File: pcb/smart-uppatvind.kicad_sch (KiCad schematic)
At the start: 70 parts, among them J1 PWR, J2 QWIIC, J3 UART_PROG, J4 FAN, Q1 IRLML9301, Q2 MMBT3904, Q3 MMBT3904, Q4 MMBT3904, Q5 Q_NMOS_GSD, SW1 EN, SW2 MAIN, SW3 BOOT, SW4 FILTER, U1 LDL1117S33R, U2 L7980A, U3 ESP32-C3-WROOM-02, U4 M24C02-WMN

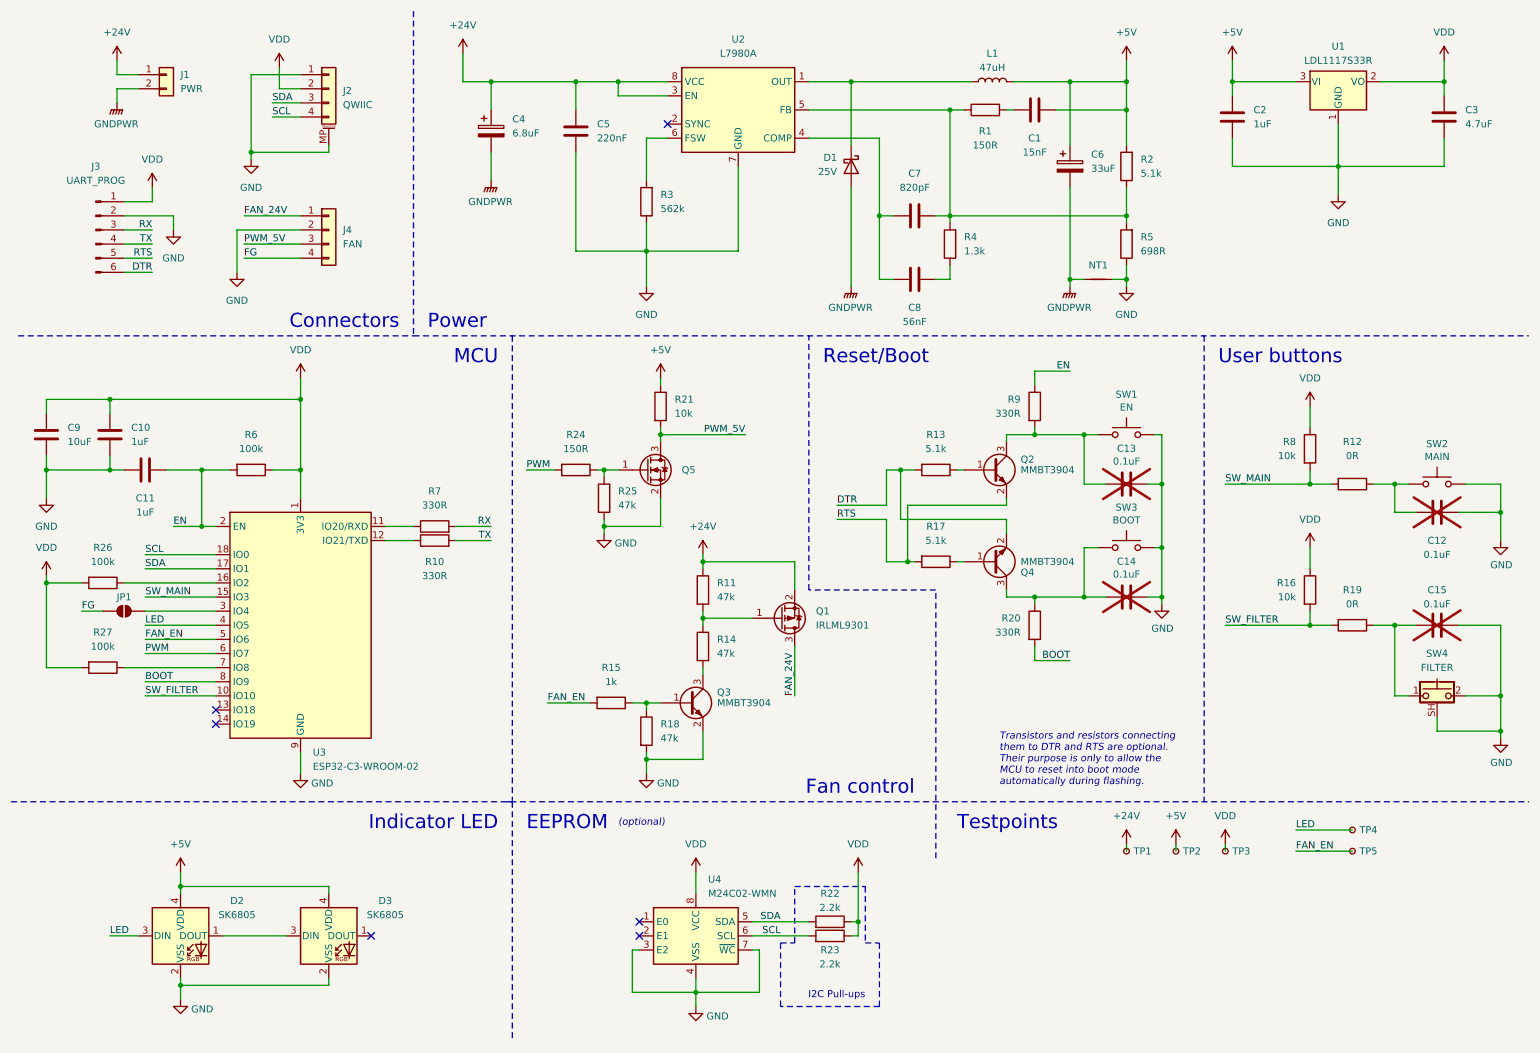
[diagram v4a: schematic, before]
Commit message: Reannotated components geographically, adjusted designator positions
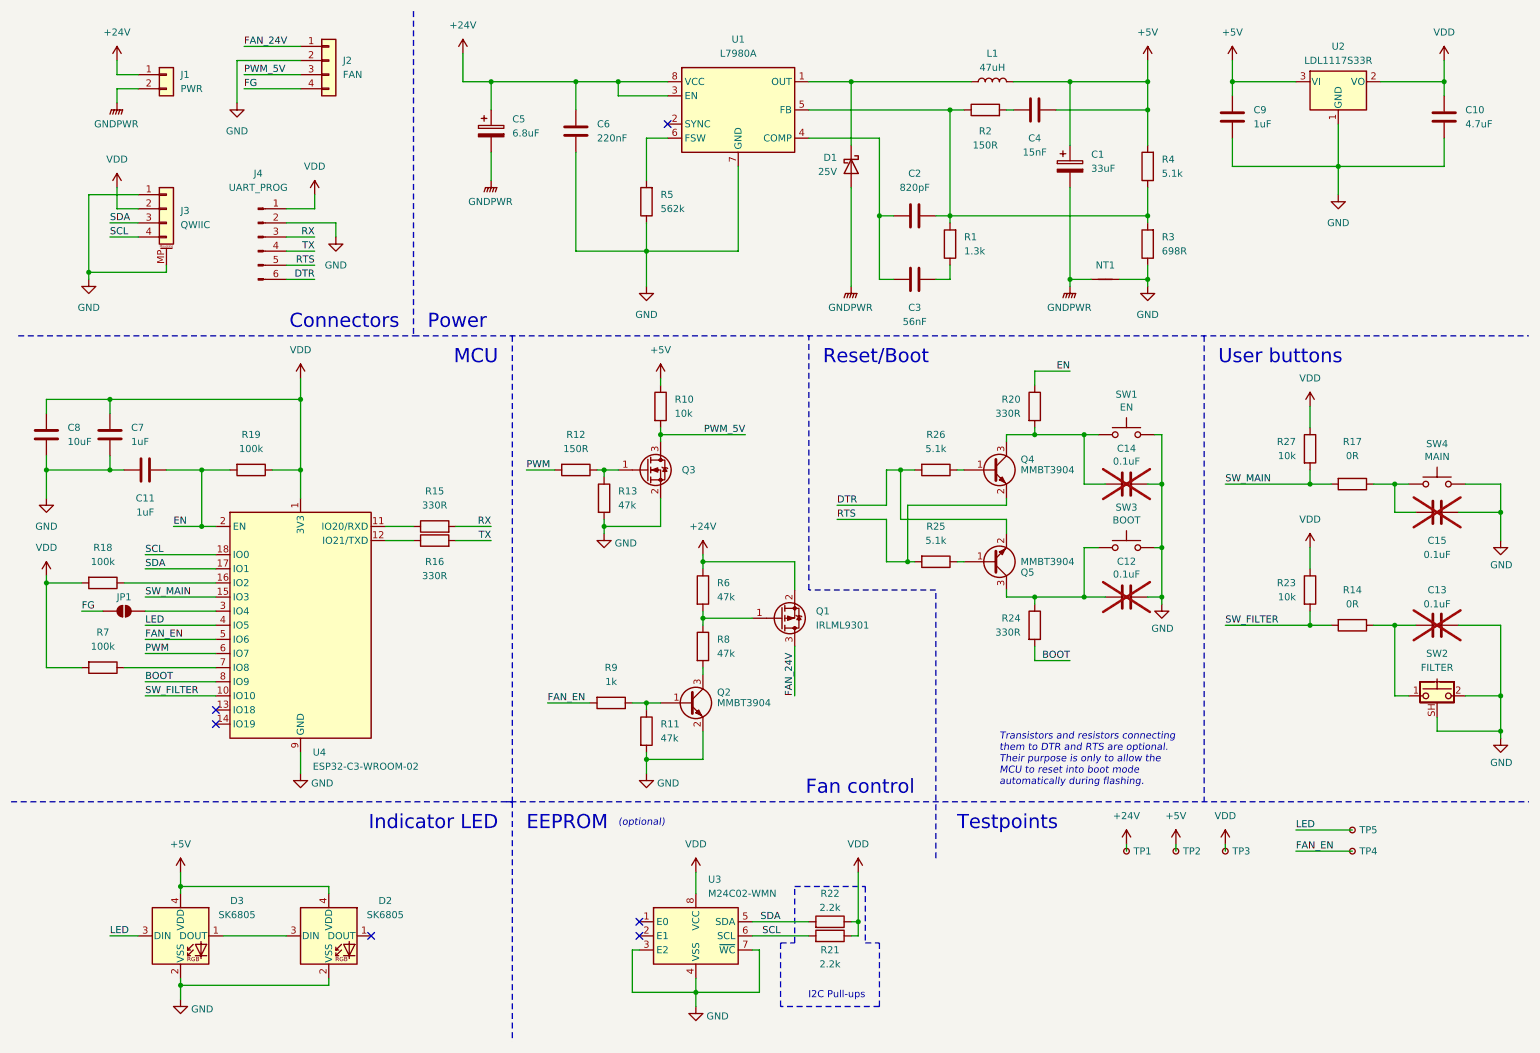
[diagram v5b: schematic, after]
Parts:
- renumbered C6 to C1, C3 to C10, C14 to C12, C15 to C13, C13 to C14, C12 to C15, C7 to C2, C8 to C3, C1 to C4, C4 to C5, C5 to C6, C10 to C7, C9 to C8, C2 to C9, D3 to D2, D2 to D3, J4 to J2, J2 to J3, J3 to J4, Q3 to Q2, Q5 to Q3, Q2 to Q4, Q4 to Q5, R4 to R1, R21 to R10, R18 to R11, R24 to R12, R25 to R13, R19 to R14, R7 to R15, R10 to R16, R12 to R17, R26 to R18, R6 to R19, R1 to R2, R9 to R20, R23 to R21, R16 to R23, R20 to R24, R17 to R25, R13 to R26, R8 to R27, R5 to R3, R2 to R4, R3 to R5, R11 to R6, R27 to R7, R14 to R8, R15 to R9, SW4 to SW2, SW2 to SW4, TP5 to TP4, TP4 to TP5, U2 to U1, U1 to U2, U4 to U3, U3 to U4
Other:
- moved on the sheet: J2, J3, J4, NT1, R3, R4
